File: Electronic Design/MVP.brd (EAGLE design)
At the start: 94.6 x 78.5 mm, 35 parts, among them IC1 ACS712ELC-5A, IC2 ATMEGA328-PU, Q1 IRF9540, Q2 IRF9540, X1 16MHz

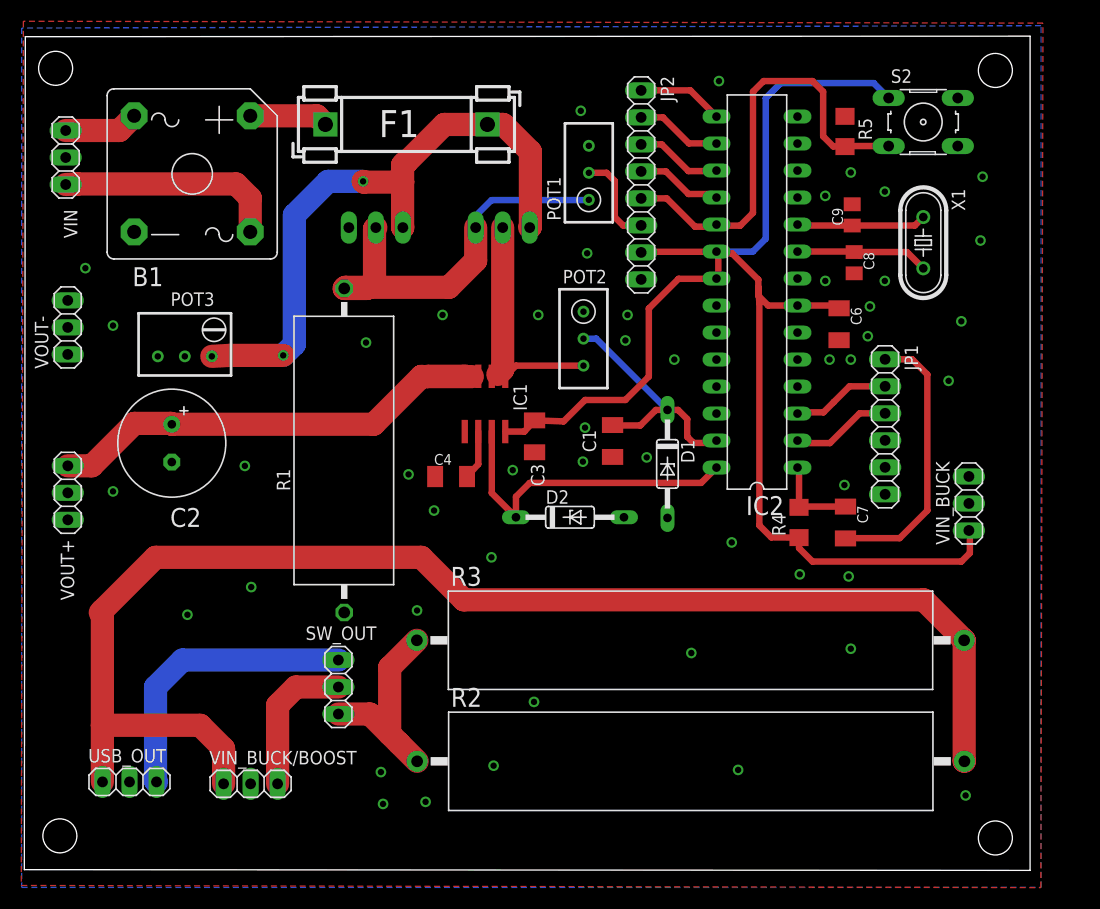
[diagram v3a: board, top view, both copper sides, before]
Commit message: flipping Q1 and Q2 back to top to save space. This is due to them never getting hot during testing so there did not seem to be a good reason for them to be on the bottom
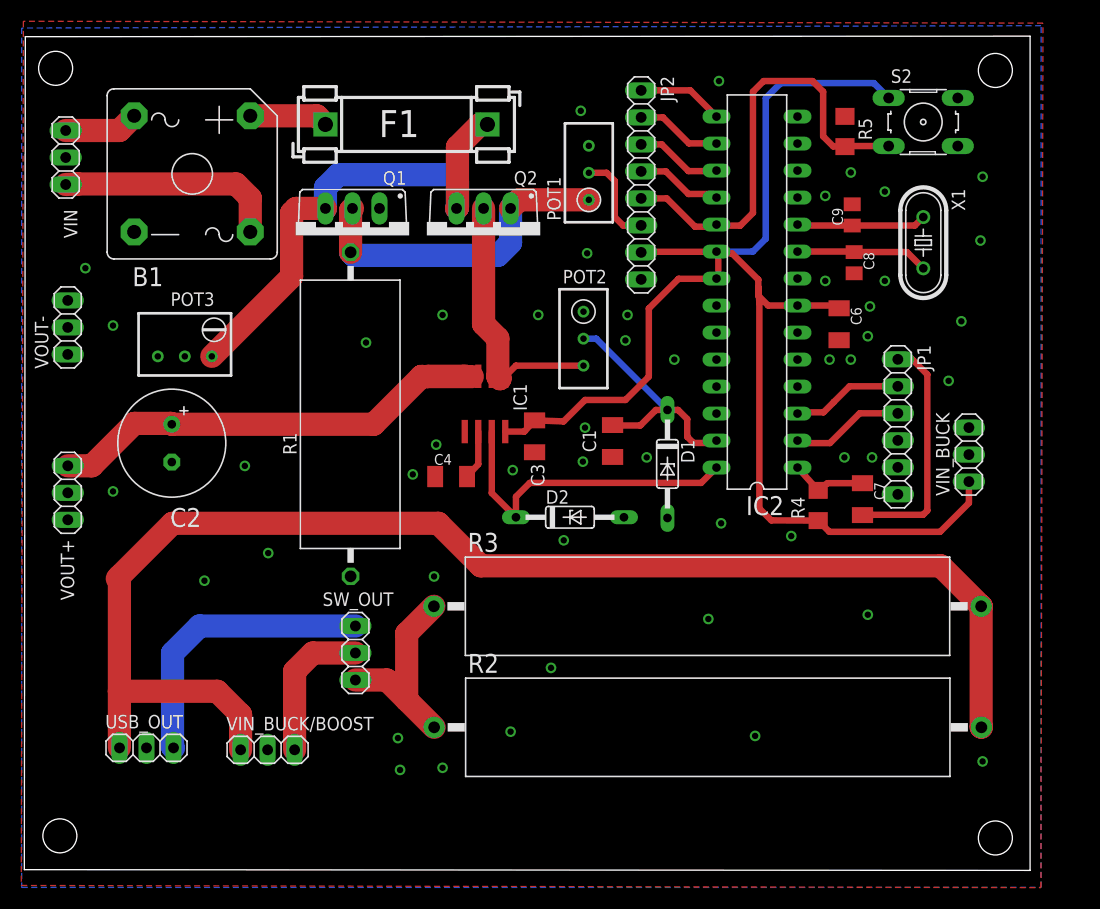
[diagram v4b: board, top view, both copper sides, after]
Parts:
- moved VIN_BUCK 4.60 mm to (89.5, 42.3)
- moved R3 3.58 mm to (64.9, 28.0)
- moved SW_OUT 3.58 mm to (31.8, 23.6)
- moved R2 3.58 mm to (64.9, 16.6)
- moved USB_OUT 3.58 mm to (12.2, 14.7)
- moved VIN_BUCK/BOOST 3.58 mm to (23.5, 14.5)
- moved R1 3.45 mm to (31.3, 46.1)
- moved Q1 2.84 mm to (31.5, 62.9), flipped to the top
- moved C7 2.72 mm to (79.5, 38.1)
- moved Q2 2.55 mm to (43.9, 62.9), flipped to the top
- moved R4 2.41 mm to (75.3, 37.5)
- moved JP1 1.20 mm to (82.8, 44.9)
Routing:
- net N$10: track 59.6 -> 47.2 mm, vias 2 -> 0
- net N$35: track 37.1 -> 30.8 mm
- net N$14: track 26.1 -> 22.4 mm
- net N$3: track 21.8 -> 24.6 mm
- net +5V: track 131.6 -> 129.5 mm
- net N$5: track 9.50 -> 10.7 mm
- net N$4: track 9.30 -> 10.5 mm
- net N$17: track 8.20 -> 7.29 mm

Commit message: made PCB a bit smaller
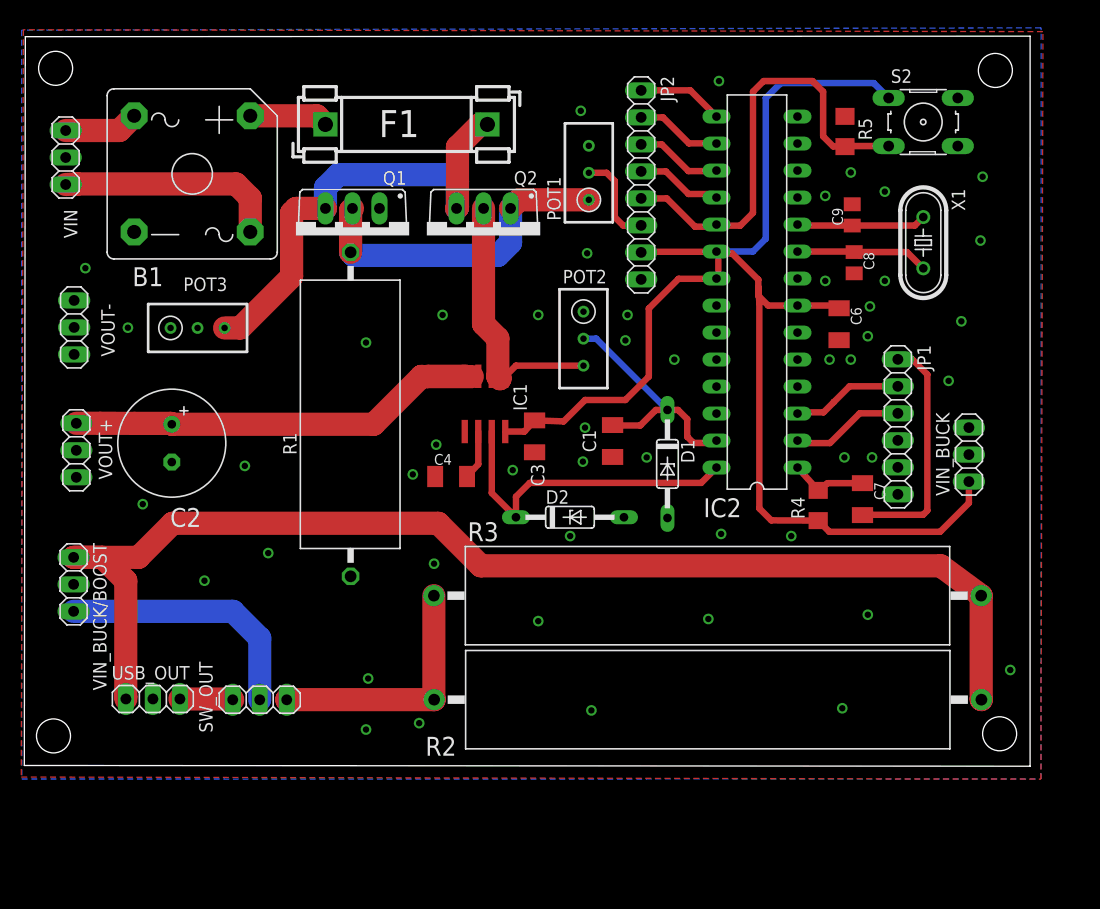
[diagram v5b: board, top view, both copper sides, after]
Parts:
- POT3: device resistor:RTRIM3299W -> resistor:RTRIM3296W
- moved VIN_BUCK/BOOST 24.0 mm to (5.29, 30.1), turned to 270 degrees
- moved SW_OUT 10.0 mm to (22.8, 19.2), turned to 0 degrees
- moved USB_OUT 4.64 mm to (12.8, 19.3)
- moved VOUT+ 4.08 mm to (5.55, 42.7)
- moved R2 2.60 mm to (64.9, 19.2)
- moved POT3 1.84 mm to (17.0, 54.2)
- moved R3 1.00 mm to (64.9, 29.0)
- moved VOUT- 0.60 mm to (5.34, 54.2)
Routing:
- net N$25: track 27.2 -> 5.00 mm
- net N$23: track 129.9 -> 116.0 mm
- net N$22: track 13.8 -> 24.4 mm
- net N$24: track 19.1 -> 23.7 mm
- net M1S: track 45.7 -> 43.3 mm
- net N$10: track 47.2 -> 44.9 mm
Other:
- board size 94.6 x 78.5 mm -> 94.6 x 68.7 mm

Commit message: changed all pin headers from 7.62mm pitch to 5.08mm pitch
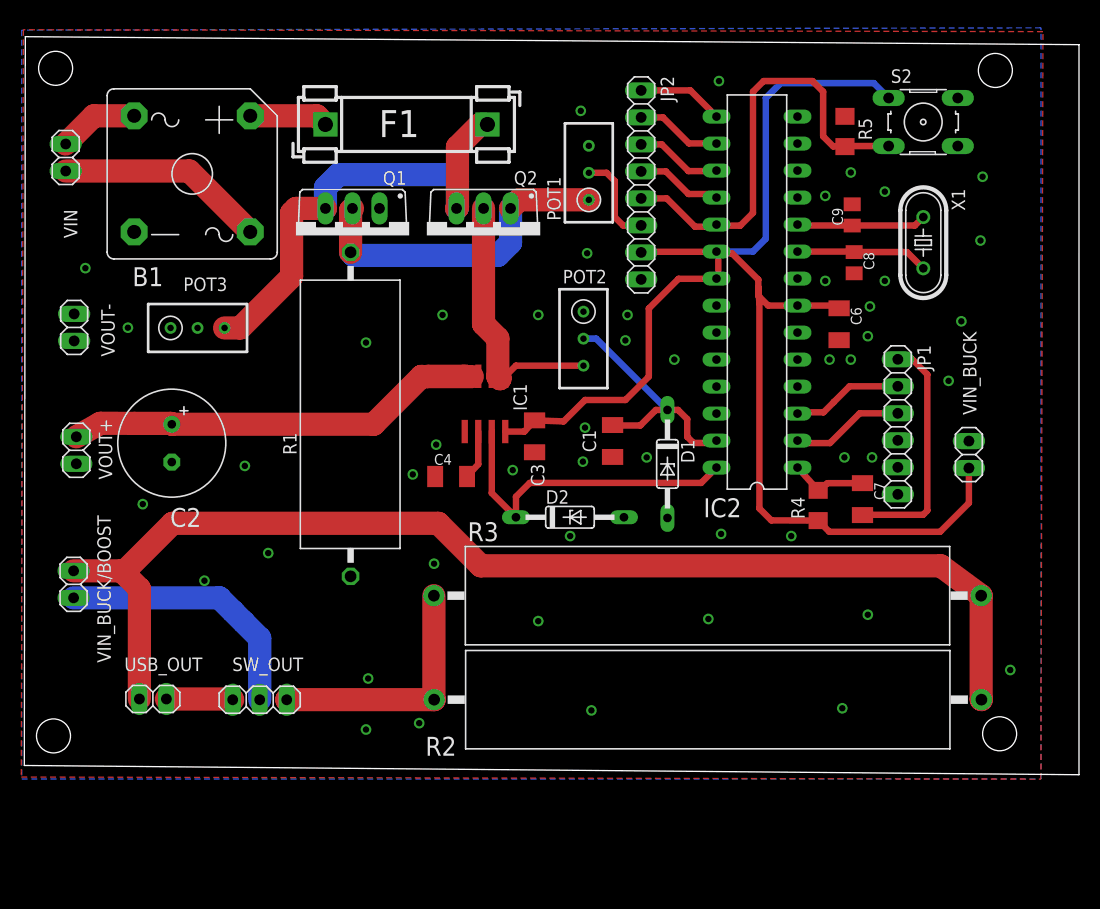
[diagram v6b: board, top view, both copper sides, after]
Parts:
- USB_OUT, VIN, VIN_BUCK, VIN_BUCK/BOOST, VOUT+, VOUT-: device pinhead:1X03 -> pinhead:1X02
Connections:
- net GND: now also VIN_BUCK.2, VOUT-.2; no longer VIN_BUCK.3, VOUT-.3
- net M1S: now also VOUT+.2; no longer VOUT+.3
- net N$19: now also VIN.2; no longer VIN.3
- net N$22: now also VIN_BUCK/BOOST.2; no longer VIN_BUCK/BOOST.3
- net N$25: now also USB_OUT.2; no longer USB_OUT.3
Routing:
- net N$23: track 116.0 -> 112.3 mm
- net N$19: track 21.1 -> 19.7 mm
- net +5V: track 129.5 -> 130.8 mm
- net N$25: track 5.00 -> 6.27 mm
- net N$22: track 24.4 -> 24.9 mm
- net N$20: track 7.01 -> 7.54 mm
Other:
- board size 94.6 x 68.7 mm -> 99.2 x 69.4 mm

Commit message: resolved clearnace issues and sorted a connection issue between pot3 and Q1
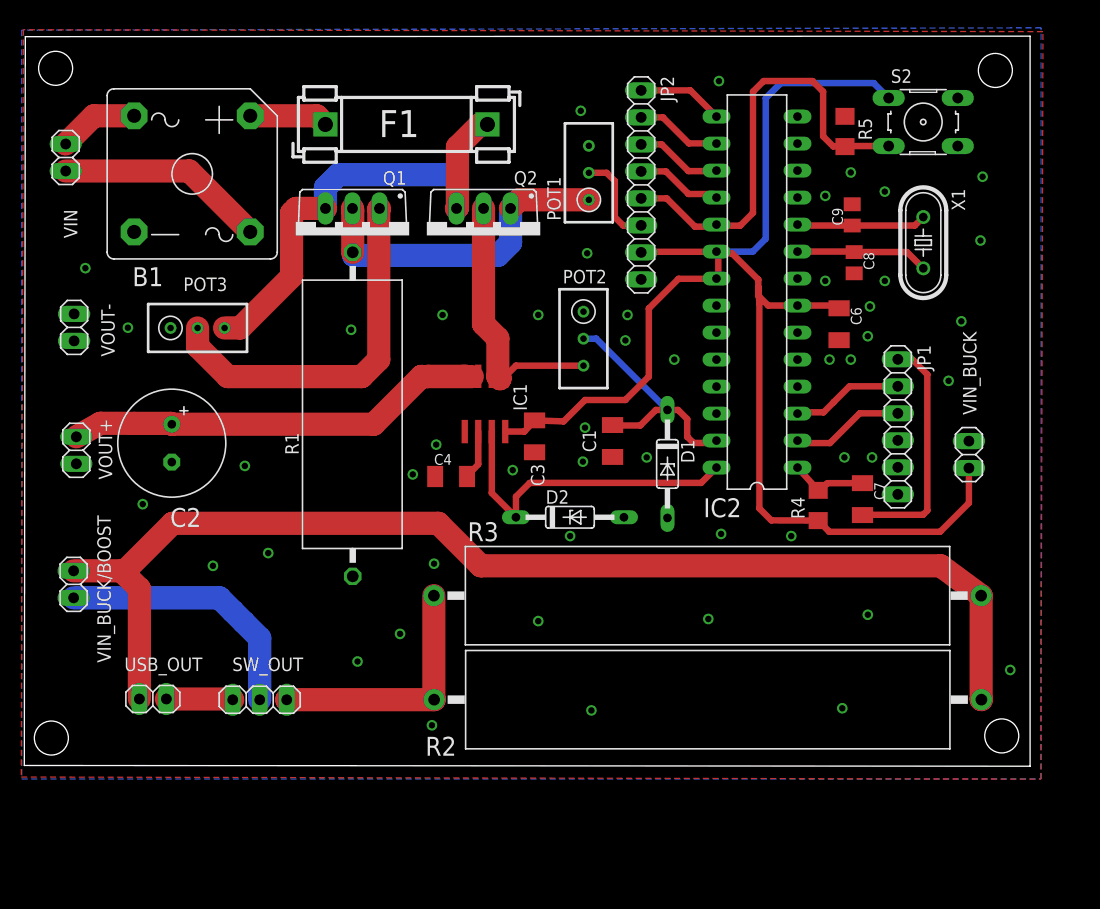
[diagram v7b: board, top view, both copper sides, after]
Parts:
- moved R1 0.20 mm to (31.5, 46.1)
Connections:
- new net N$7: POT3.2, Q1.G
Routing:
- net N$7: track 0.00 -> 34.9 mm
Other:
- board size 99.2 x 69.4 mm -> 94.6 x 68.7 mm
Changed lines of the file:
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@@
 <board>
 <plain>
-<wire x1="0.656940625" y1="13.0193125" x2="99.864721875" y2="12.1491875" width="0" layer="20"/>
-<wire x1="99.864721875" y1="12.1491875" x2="99.867225" y2="80.82396875" width="0" layer="20"/>
-<wire x1="99.867225" y1="80.82396875" x2="0.75049375" y2="81.57389375" width="0" layer="20"/>
+<wire x1="0.656940625" y1="13.0193125" x2="95.264721875" y2="12.9491875" width="0" layer="20"/>
+<wire x1="95.264721875" y1="12.9491875" x2="95.267225" y2="81.62396875" width="0" layer="20"/>
+<wire x1="95.267225" y1="81.62396875" x2="0.75049375" y2="81.57389375" width="0" layer="20"/>
 <wire x1="0.75049375" y1="81.57389375" x2="0.656940625" y2="13.0193125" width="0" layer="20"/>
 <hole x="3.6" y="78.6" drill="3.2"/>
 <hole x="92" y="78.4" drill="3.2"/>
-<hole x="3.4" y="15.8" drill="3.2"/>
-<hole x="92.4" y="16" drill="3.2"/>
+<hole x="3.2" y="15.6" drill="3.2"/>
+<hole x="92.6" y="15.8" drill="3.2"/>
 </plain>
 <attributes>
@@
 <attribute name="VALUE" x="14.41450625" y="50.1300625" size="1.27" layer="27"/>
 </element>
-<element name="R1" library="resistor" package="VTA52" value="1k" x="31.34895" y="46.051521875" rot="R90"/>
+<element name="R1" library="resistor" package="VTA52" value="1k" x="31.54895" y="46.051521875" rot="R90"/>
 <element name="VIN" library="pinhead" package="1X02" value="" x="4.548721875" y="70.209796875" smashed="yes" rot="R270">
 <attribute name="NAME" x="4.377521875" y="65.325996875" size="1.27" layer="25" ratio="10" rot="R270"/>
@@
 <via x="77.6" y="18.4" extent="1-16" drill="0.6" shape="square"/>
 <via x="54" y="18.2" extent="1-16" drill="0.6" shape="square"/>
-<via x="37.8" y="17" extent="1-16" drill="0.6" shape="square"/>
-<via x="32.8" y="16.4" extent="1-16" drill="0.6" shape="square"/>
-<via x="17.6" y="30.4" extent="1-16" drill="0.6" shape="square"/>
+<via x="36" y="25.4" extent="1-16" drill="0.6" shape="square"/>
+<via x="39" y="16.8" extent="1-16" drill="0.6" shape="square"/>
+<via x="18.4" y="31.8" extent="1-16" drill="0.6" shape="square"/>
 <via x="23.6" y="33" extent="1-16" drill="0.6" shape="square"/>
 <via x="39.2" y="32" extent="1-16" drill="0.6" shape="square"/>
-<via x="33" y="21.2" extent="1-16" drill="0.6" shape="square"/>
+<via x="32" y="22.8" extent="1-16" drill="0.6" shape="square"/>
 <via x="80.4" y="42" extent="1-16" drill="0.6" shape="square"/>
 <via x="65" y="26.8" extent="1-16" drill="0.6" shape="square"/>
@@
 <via x="49" y="55.4" extent="1-16" drill="0.6" shape="square"/>
 <via x="57.2" y="53" extent="1-16" drill="0.6" shape="square"/>
-<via x="32.8" y="52.8" extent="1-16" drill="0.6" shape="square"/>
+<via x="31.4" y="54" extent="1-16" drill="0.6" shape="square"/>
 <via x="6.4" y="59.8" extent="1-16" drill="0.6" shape="square"/>
 <via x="10.4" y="54.2" extent="1-16" drill="0.6" shape="square"/>
@@
 <contactref element="Q2" pad="G"/>
 <contactref element="POT1" pad="1"/>
-<wire x1="31.34895" y1="61.291521875" x2="31.34895" y2="65.244378125" width="2.1844" layer="1"/>
-<wire x1="31.34895" y1="65.244378125" x2="31.524390625" y2="65.41981875" width="2.1844" layer="1"/>
+<wire x1="31.54895" y1="61.291521875" x2="31.54895" y2="65.244378125" width="2.1844" layer="1"/>
+<wire x1="31.54895" y1="65.244378125" x2="31.524390625" y2="65.41981875" width="2.1844" layer="1"/>
 <wire x1="53.759509375" y1="66.231371875" x2="47.20594375" y2="66.231371875" width="2.1844" layer="1"/>
 <wire x1="47.20594375" y1="66.231371875" x2="46.394390625" y2="65.41981875" width="2.1844" layer="1"/>
@@
 <wire x1="46.394390625" y1="62.194390625" x2="45.2" y2="61" width="2.1844" layer="16"/>
 <wire x1="45.2" y1="61" x2="31.640471875" y2="61" width="2.1844" layer="16"/>
-<wire x1="31.640471875" y1="61" x2="31.34895" y2="61.291521875" width="2.1844" layer="16"/>
+<wire x1="31.640471875" y1="61" x2="31.54895" y2="61.291521875" width="2.1844" layer="16"/>
 </signal>
 <signal name="+5V">
@@
 <wire x1="43.3579625" y1="41.3579625" x2="42.3" y2="40.2" width="0.6096" layer="1"/>
 </signal>
+<signal name="N$7">
+<contactref element="Q1" pad="G"/>
+<contactref element="POT3" pad="2"/>
+<wire x1="16.95450625" y1="54.1750625" x2="16.95450625" y2="52.44549375" width="2.1844" layer="1"/>
+<wire x1="16.95450625" y1="52.44549375" x2="19.8" y2="49.6" width="2.1844" layer="1"/>
+<wire x1="19.8" y1="49.6" x2="32.4" y2="49.6" width="2.1844" layer="1"/>
+<wire x1="32.4" y1="49.6" x2="34" y2="51.2" width="2.1844" layer="1"/>
+<wire x1="34" y1="51.2" x2="34" y2="65.355428125" width="2.1844" layer="1"/>
+<wire x1="34" y1="65.355428125" x2="34.064390625" y2="65.41981875" width="2.1844" layer="1"/>
+</signal>
 </signals>
